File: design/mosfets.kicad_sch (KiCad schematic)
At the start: 15 parts, among them Q1 IRFS7530, Q2 IRFS7530, Q3 IRFS7530, Q4 IRFS7530, Q5 IRFS7530, Q6 IRFS7530

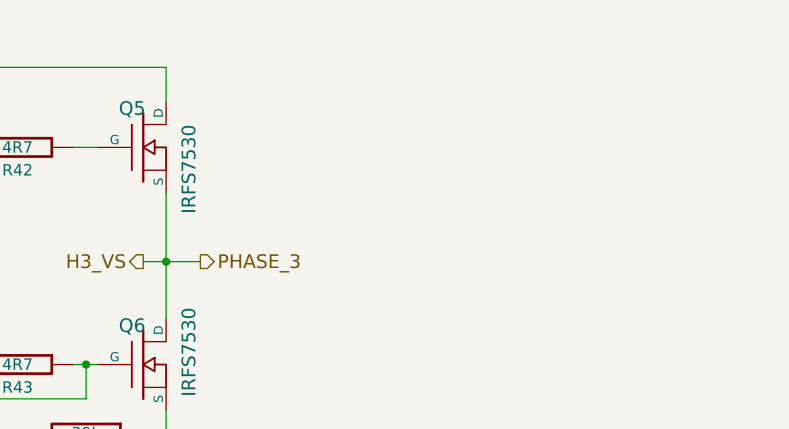
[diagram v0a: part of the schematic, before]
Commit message: extended board include input power caps and holes for wires
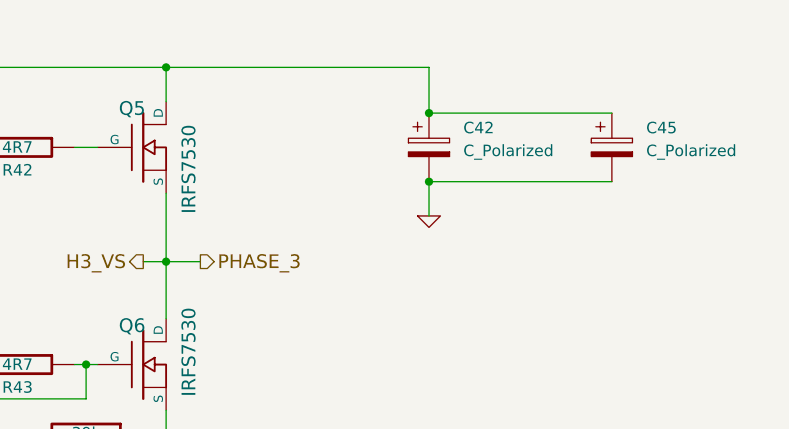
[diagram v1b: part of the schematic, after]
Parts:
- added C42, C45: C_Polarized, Capacitor_THT:CP_Radial_D13.0mm_P5.00mm, symbol Device:C_Polarized
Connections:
- net V_SUPPLY: now also C42.1, C45.1
- new net GND: C42.2, C45.2

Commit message: v 4.13 produced by jlcpcb
Some serious issues with usb connectors facing the caps. Working fine
otherwise
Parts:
- C42, C45: JLCPCB (none) -> c106632
- Q1, Q2, Q3, Q4, Q5, Q6: JLCPCB (none) -> C445669
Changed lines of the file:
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@@
 (kicad_sch
-	(version 20231120)
+	(version 20250114)
 	(generator "eeschema")
-	(generator_version "8.0")
+	(generator_version "9.0")
 	(paper "A4")
 	(title_block
 		(title "BLDC Driver 4.11")
 		(date "21 aug 2015")
-		(rev "4.12")
+		(rev "${version}")
 		(company "Benjamin Vedder")
 	)
@@
 		(shape input)
 		(at 102.87 95.25 180)
-		(fields_autoplaced yes)
 		(effects
 			(font
@@
 		(shape output)
 		(at 132.08 83.82 0)
-		(fields_autoplaced yes)
 		(effects
 			(font
@@
 		(shape output)
 		(at 205.74 83.82 180)
-		(fields_autoplaced yes)
 		(effects
 			(font
@@
 		(shape passive)
 		(at 167.64 114.3 270)
-		(fields_autoplaced yes)
 		(effects
 			(font
@@
 		(shape input)
 		(at 142.24 71.12 180)
-		(fields_autoplaced yes)
 		(effects
 			(font
@@
 		(shape input)
 		(at 143.51 95.25 180)
-		(fields_autoplaced yes)
 		(effects
 			(font
@@
 		(shape passive)
 		(at 128.27 114.3 270)
-		(fields_autoplaced yes)
 		(effects
 			(font
@@
 		(shape output)
 		(at 171.45 83.82 0)
-		(fields_autoplaced yes)
 		(effects
 			(font
@@
 		(shape output)
 		(at 125.73 83.82 180)
-		(fields_autoplaced yes)
 		(effects
 			(font
@@
 		(shape input)
 		(at 182.88 71.12 180)
-		(fields_autoplaced yes)
 		(effects
 			(font
@@
 		(shape input)
 		(at 102.87 71.12 180)
-		(fields_autoplaced yes)
 		(effects
 			(font
@@
 		(shape output)
 		(at 165.1 83.82 180)
-		(fields_autoplaced yes)
 		(effects
 			(font
@@
 		(shape passive)
 		(at 208.28 114.3 270)
-		(fields_autoplaced yes)
 		(effects
 			(font
@@
 		(shape input)
 		(at 184.15 95.25 180)
-		(fields_autoplaced yes)
 		(effects
 			(font
@@
 		(shape output)
 		(at 212.09 83.82 0)
-		(fields_autoplaced yes)
 		(effects
 			(font
@@
 			)
 		)
+		(property "JLCPCB" "C445669"
+			(at 125.73 71.12 0)
+			(effects
+				(font
+					(size 1.27 1.27)
+				)
+				(hide yes)
+			)
+		)
 		(pin "D"
 		)
@@
 			)
 		)
+		(property "JLCPCB" "C445669"
+			(at 125.73 95.25 0)
+			(effects
+				(font
+					(size 1.27 1.27)
+				)
+				(hide yes)
+			)
+		)
 		(pin "D"
 		)
@@
 			)
 		)
+		(property "JLCPCB" "C445669"
+			(at 165.1 95.25 0)
+			(effects
+				(font
+					(size 1.27 1.27)
+				)
+				(hide yes)
+			)
+		)
 		(pin "D"
 		)
@@
 			)
 		)
+		(property "JLCPCB" "C445669"
+			(at 165.1 71.12 0)
+			(effects
+				(font
+					(size 1.27 1.27)
+				)
+				(hide yes)
+			)
+		)
 		(pin "D"
 		)
@@
 			)
 		)
+		(property "JLCPCB" "C445669"
+			(at 205.74 71.12 0)
+			(effects
+				(font
+					(size 1.27 1.27)
+				)
+				(hide yes)
+			)
+		)
 		(pin "D"
 		)
@@
 		)
 		(property "Description" ""
+			(at 205.74 95.25 0)
+			(effects
+				(font
+					(size 1.27 1.27)
+				)
+				(hide yes)
+			)
+		)
+		(property "JLCPCB" "C445669"
 			(at 205.74 95.25 0)
 			(effects
@@
 			)
 		)
+		(property "JLCPCB" "c106632"
+			(at 237.49 71.12 0)
+			(effects
+				(font
+					(size 1.27 1.27)
+				)
+				(hide yes)
+			)
+		)
+		(property "Field6" ""
+			(at 237.49 71.12 0)
+			(effects
+				(font
+					(size 1.27 1.27)
+				)
+				(hide yes)
+			)
+		)
 		(pin "1"
 		)
@@
 			(at 257.81 71.12 0)
 			(effects
+				(font
+					(size 1.27 1.27)
+				)
+				(hide yes)
+			)
+		)
+		(property "JLCPCB" "c106632"
+			(at 257.81 71.12 0)
+			(effects
+				(font
+					(size 1.27 1.27)
+				)
+				(hide yes)
+			)
+		)
+		(property "Field6" ""
+			(at 257.81 71.12 0)
+			(effects
